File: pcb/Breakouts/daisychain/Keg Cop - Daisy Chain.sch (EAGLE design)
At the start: 3 parts

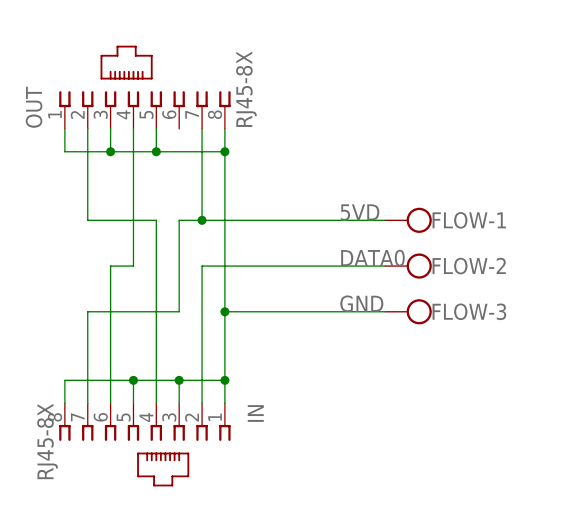
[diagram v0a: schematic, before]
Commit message: Add series resistor
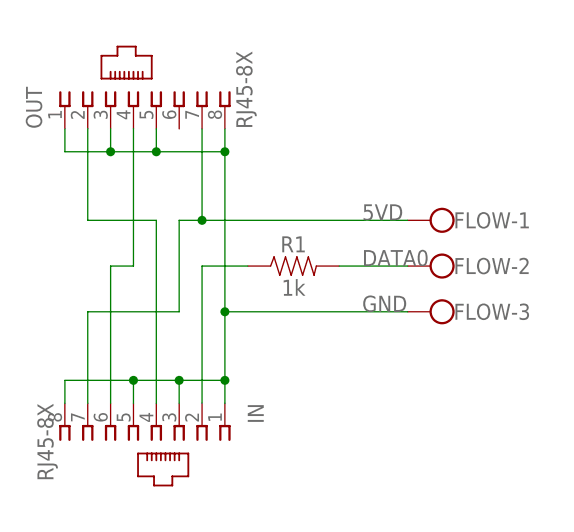
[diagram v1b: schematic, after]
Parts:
- added R1: 1k, SparkFun-Resistors:1KOHM-HORIZ-1/4W-5%
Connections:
- new net N$1: FLOW-2.KL, R1.2
- net DATA0: now also R1.1; no longer FLOW-2.KL
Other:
- moved on the sheet: FLOW-1, FLOW-2, FLOW-3
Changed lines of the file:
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@@
 <part name="OUT" library="con-tycoelectronics" library_urn="urn:adsk.eagle:library:193" deviceset="RJ45" device="" package3d_urn="urn:adsk.eagle:package:10660/1" technology="-8X"/>
 <part name="FLOW" library="con-wago-500" library_urn="urn:adsk.eagle:library:195" deviceset="W237-103" device="" package3d_urn="urn:adsk.eagle:package:10691/1"/>
+<part name="R1" library="SparkFun-Resistors" library_urn="urn:adsk.eagle:library:532" deviceset="1KOHM" device="-HORIZ-1/4W-5%" package3d_urn="urn:adsk.eagle:package:39658/1" value="1k"/>
 </parts>
 <sheets>
@@
 <attribute name="VALUE" x="74.168" y="66.04" size="1.778" layer="96" rot="R90"/>
 </instance>
-<instance part="FLOW" gate="-1" x="93.98" y="55.88" smashed="yes" rot="R180">
-<attribute name="NAME" x="93.98" y="54.991" size="1.778" layer="95"/>
+<instance part="FLOW" gate="-1" x="96.52" y="55.88" smashed="yes" rot="R180">
+<attribute name="NAME" x="96.52" y="54.991" size="1.778" layer="95"/>
 </instance>
-<instance part="FLOW" gate="-2" x="93.98" y="50.8" smashed="yes" rot="R180">
-<attribute name="NAME" x="93.98" y="49.911" size="1.778" layer="95"/>
+<instance part="FLOW" gate="-2" x="96.52" y="50.8" smashed="yes" rot="R180">
+<attribute name="NAME" x="96.52" y="49.911" size="1.778" layer="95"/>
 </instance>
-<instance part="FLOW" gate="-3" x="93.98" y="45.72" smashed="yes" rot="R180">
-<attribute name="VALUE" x="96.52" y="49.403" size="1.778" layer="96" rot="R180"/>
-<attribute name="NAME" x="93.98" y="44.831" size="1.778" layer="95"/>
+<instance part="FLOW" gate="-3" x="96.52" y="45.72" smashed="yes" rot="R180">
+<attribute name="VALUE" x="99.06" y="49.403" size="1.778" layer="96" rot="R180"/>
+<attribute name="NAME" x="96.52" y="44.831" size="1.778" layer="95"/>
+</instance>
+<instance part="R1" gate="G$1" x="78.74" y="50.8" smashed="yes">
+<attribute name="NAME" x="78.74" y="52.324" size="1.778" layer="95" font="vector" align="bottom-center"/>
+<attribute name="VALUE" x="78.74" y="49.276" size="1.778" layer="96" font="vector" align="top-center"/>
 </instance>
 </instances>
@@
 <junction x="71.12" y="63.5"/>
 <pinref part="FLOW" gate="-3" pin="KL"/>
-<wire x1="88.9" y1="45.72" x2="71.12" y2="45.72" width="0.1524" layer="91"/>
+<wire x1="91.44" y1="45.72" x2="71.12" y2="45.72" width="0.1524" layer="91"/>
 <junction x="71.12" y="45.72"/>
-<label x="83.82" y="45.72" size="1.778" layer="95"/>
+<label x="86.36" y="45.72" size="1.778" layer="95"/>
 </segment>
 </net>
@@
 <pinref part="IN" gate="G$1" pin="2"/>
 <wire x1="68.58" y1="35.56" x2="68.58" y2="50.8" width="0.1524" layer="91"/>
-<pinref part="FLOW" gate="-2" pin="KL"/>
-<wire x1="68.58" y1="50.8" x2="88.9" y2="50.8" width="0.1524" layer="91"/>
-<label x="83.82" y="50.8" size="1.778" layer="95"/>
+<label x="86.36" y="50.8" size="1.778" layer="95"/>
+<pinref part="R1" gate="G$1" pin="1"/>
+<wire x1="68.58" y1="50.8" x2="73.66" y2="50.8" width="0.1524" layer="91"/>
 </segment>
 </net>
@@
 <wire x1="68.58" y1="55.88" x2="68.58" y2="66.04" width="0.1524" layer="91"/>
 <pinref part="FLOW" gate="-1" pin="KL"/>
-<wire x1="88.9" y1="55.88" x2="68.58" y2="55.88" width="0.1524" layer="91"/>
+<wire x1="91.44" y1="55.88" x2="68.58" y2="55.88" width="0.1524" layer="91"/>
 <junction x="68.58" y="55.88"/>
-<label x="83.82" y="55.88" size="1.778" layer="95"/>
+<label x="86.36" y="55.88" size="1.778" layer="95"/>
 </segment>
 </net>
@@
 </segment>
 </net>
+<net name="N$1" class="0">
+<segment>
+<pinref part="FLOW" gate="-2" pin="KL"/>
+<wire x1="91.44" y1="50.8" x2="83.82" y2="50.8" width="0.1524" layer="91"/>
+<pinref part="R1" gate="G$1" pin="2"/>
+</segment>
+</net>
 </nets>
 </sheet>
 </sheets>
+<errors>
+</errors>
 </schematic>
 </drawing>

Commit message: Updated Daisy Chain
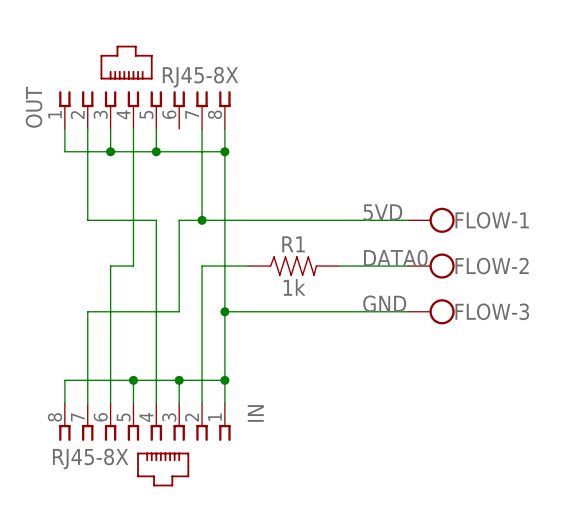
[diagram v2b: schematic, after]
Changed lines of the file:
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@@
 <instance part="IN" gate="G$1" x="63.5" y="33.02" smashed="yes" rot="R270">
 <attribute name="NAME" x="73.66" y="35.56" size="1.778" layer="95" rot="R270"/>
-<attribute name="VALUE" x="50.292" y="35.56" size="1.778" layer="96" rot="R270"/>
+<attribute name="VALUE" x="60.452" y="30.48" size="1.778" layer="96" rot="R180"/>
 </instance>
 <instance part="OUT" gate="G$1" x="60.96" y="68.58" smashed="yes" rot="R90">
 <attribute name="NAME" x="50.8" y="66.04" size="1.778" layer="95" rot="R90"/>
-<attribute name="VALUE" x="74.168" y="66.04" size="1.778" layer="96" rot="R90"/>
+<attribute name="VALUE" x="64.008" y="71.12" size="1.778" layer="96"/>
 </instance>
 <instance part="FLOW" gate="-1" x="96.52" y="55.88" smashed="yes" rot="R180">
